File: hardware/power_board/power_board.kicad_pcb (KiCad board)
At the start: 2 copper layers, 45.8 x 25 mm, 21 parts, among them J1 Barrel_Jack, J2 Conn_01x05_Male, U1 LM1117-ADJ, U2 LM1117-ADJ, U3 LM1117-ADJ, U4 LM2776

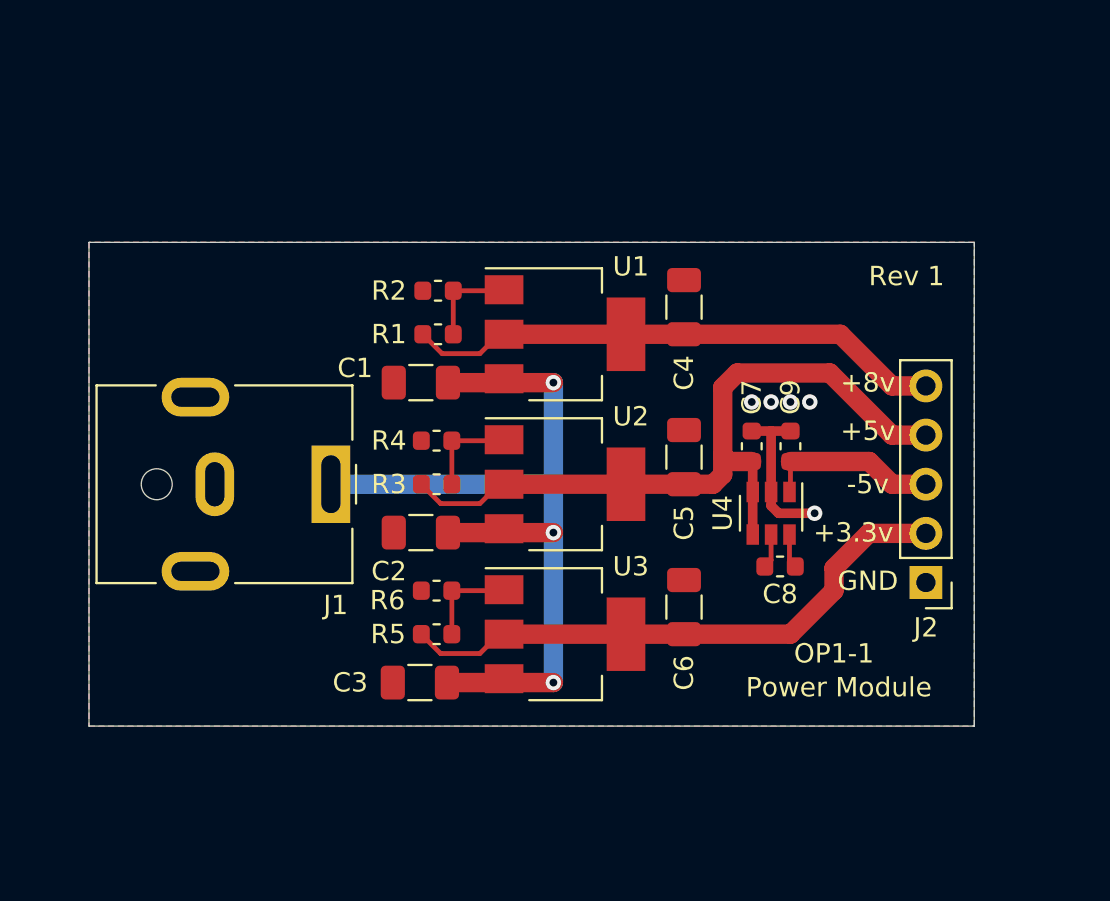
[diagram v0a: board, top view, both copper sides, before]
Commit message: Made the board design a little more spacious
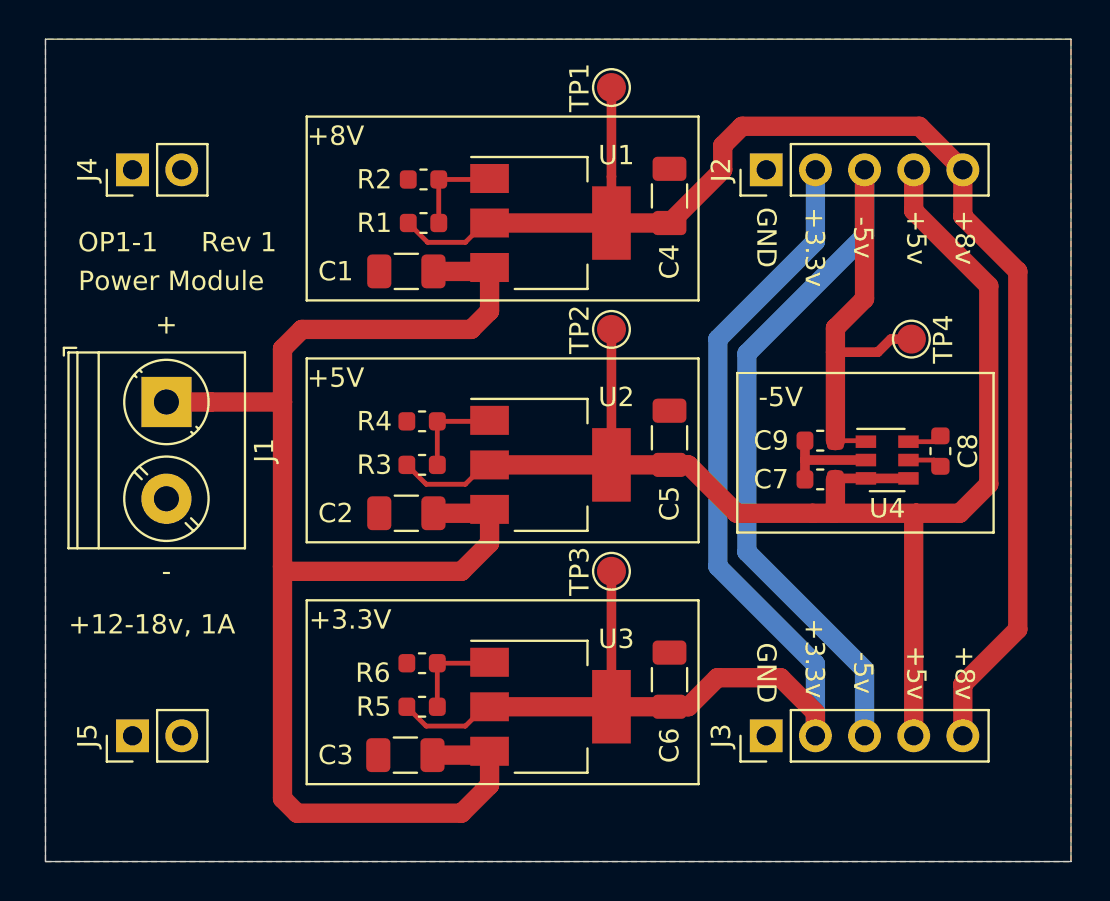
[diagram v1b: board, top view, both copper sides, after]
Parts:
- added J3: Conn_01x05_Male, Connector_PinHeader_2.54mm:PinHeader_1x05_P2.54mm_Vertical, F.Cu at (139.2, 100.5)
- added J4: Conn_01x02_Male, Connector_PinHeader_2.54mm:PinHeader_1x02_P2.54mm_Vertical, F.Cu at (106.5, 71.2)
- added J5: Conn_01x02_Male, Connector_PinHeader_2.54mm:PinHeader_1x02_P2.54mm_Vertical, F.Cu at (106.5, 100.5)
- added TP1: TestPoint, TestPoint:TestPoint_Pad_D1.5mm, F.Cu at (131.2, 67.0)
- added TP2: TestPoint, TestPoint:TestPoint_Pad_D1.5mm, F.Cu at (131.2, 79.5)
- added TP3: TestPoint, TestPoint:TestPoint_Pad_D1.5mm, F.Cu at (131.2, 92.0)
- added TP4: TestPoint, TestPoint:TestPoint_Pad_D1.5mm, F.Cu at (146.8, 80.0)
- J1: value Barrel_Jack -> Screw_Terminal_01x02; footprint Connector_BarrelJack:BarrelJack_CUI_PJ-063AH_Horizontal -> TerminalBlock_Phoenix:TerminalBlock_Phoenix_PT-1,5-2-5.0-H_1x02_P5.00mm_Horizontal
- moved J2 22.9 mm to (139.2, 71.2), turned to 90 degrees
- moved C8 10.2 mm to (148.2, 85.8), turned to 270 degrees
- moved J1 9.50 mm to (108.2, 83.2)
- moved U4 6.60 mm to (145.5, 86.2), turned to 0 degrees
- moved C1 5.80 mm to (120.7, 76.5)
- moved C4 5.80 mm to (134.2, 72.6)
- moved R1 5.80 mm to (121.5, 74.0)
- moved R2 5.80 mm to (121.5, 71.8)
- moved U1 5.80 mm to (128.1, 74.0)
- moved C7 3.93 mm to (142.0, 87.2), turned to 0 degrees
- moved C3 3.82 mm to (120.6, 101.5)
- moved C6 3.82 mm to (134.2, 97.6)
- moved R5 3.82 mm to (121.5, 99.0)
- moved R6 3.82 mm to (121.5, 96.8)
- moved U3 3.82 mm to (128.1, 99.0)
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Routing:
- net /-5v: track 9.08 -> 54.7 mm
- net /+8v: track 27.9 -> 71.8 mm
- net /+5v: track 38.8 -> 74.6 mm
- net Net-(C1-Pad1): track 43.9 -> 79.4 mm, vias 3 -> 0
- net /+3.3v: track 29.7 -> 64.9 mm
- net GND: track 8.27 -> 5.15 mm, vias 5 -> 0
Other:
- board size 45.8 x 25 mm -> 53 x 42.5 mm
- board text added: "+"
- board text added: "+12-18v, 1A"
- board text added: "+3.3V"
- board text added: "+5V"
- board text added: "+8V"
- board text added: "-"
- board text added: "-5V"
